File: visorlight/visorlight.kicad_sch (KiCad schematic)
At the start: 1 part

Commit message: rename
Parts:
- added J1: Conn_01x04, Connector_Wire:SolderWire-0.25sqmm_1x01_D0.65mm_OD1.7mm, symbol Connector_Generic:Conn_01x04
- LED1: symbol project_parts:LED_1010RGBC -> visorlight_parts:LED_1010RGBC
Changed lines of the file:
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@@
 (kicad_sch (version 20230121) (generator eeschema)
   (paper "A4")
-  (symbol (lib_id "project_parts:LED_1010RGBC") (at 49.53 46.99 0) (unit 1)
+  (symbol (lib_id "Connector_Generic:Conn_01x04") (at 31.75 48.26 180) (unit 1)
+    (in_bom yes) (on_board yes) (dnp no) (fields_autoplaced)
+    (property "Reference" "J1" (at 31.75 36.83 0)
+      (effects (font (size 1.27 1.27)))
+    )
+    (property "Value" "Conn_01x04" (at 31.75 39.37 0)
+      (effects (font (size 1.27 1.27)))
+    )
+    (property "Footprint" "Connector_Wire:SolderWire-0.25sqmm_1x01_D0.65mm_OD1.7mm" (at 31.75 48.26 0)
+      (effects (font (size 1.27 1.27)) hide)
+    )
+    (property "Datasheet" "~" (at 31.75 48.26 0)
+      (effects (font (size 1.27 1.27)) hide)
+    )
+    (pin "4")
+    (pin "2")
+    (pin "1")
+    (pin "3")
+    (instances
+      (project "visorlight"
+        (path "/ada48de3-1b88-4013-bdaa-c0c1b764bc21"
+          (reference "J1") (unit 1)
+        )
+      )
+    )
+  )
+  (symbol (lib_id "visorlight_parts:LED_1010RGBC") (at 49.53 46.99 0) (unit 1)
     (in_bom yes) (on_board yes) (dnp no)
     (property "Reference" "LED1" (at 44.45 40.64 0)

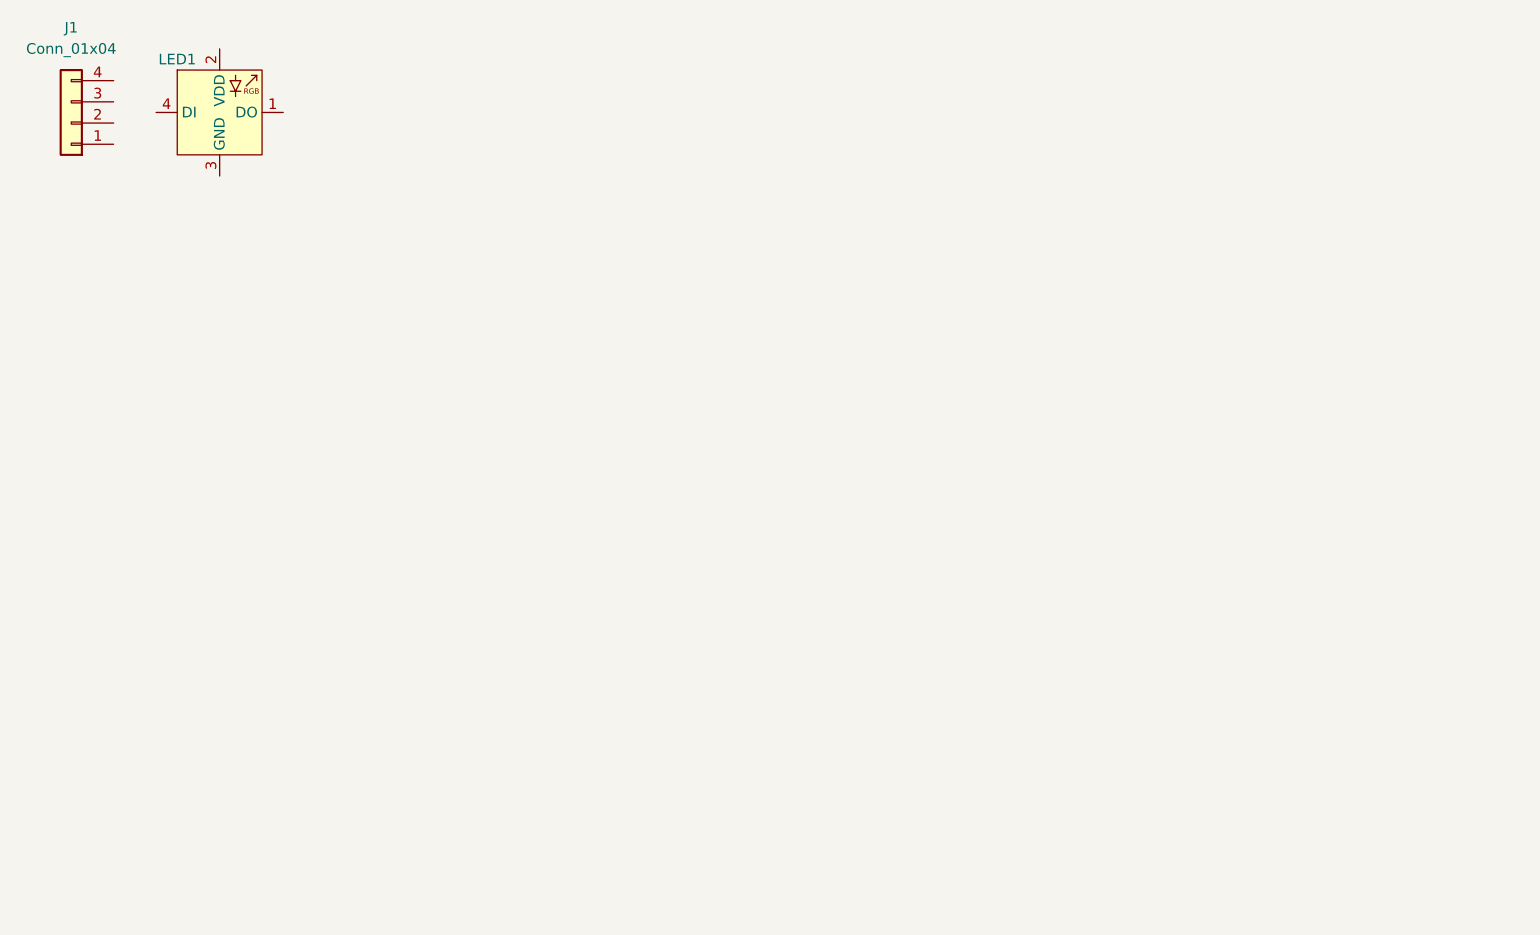
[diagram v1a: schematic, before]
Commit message: moar leds
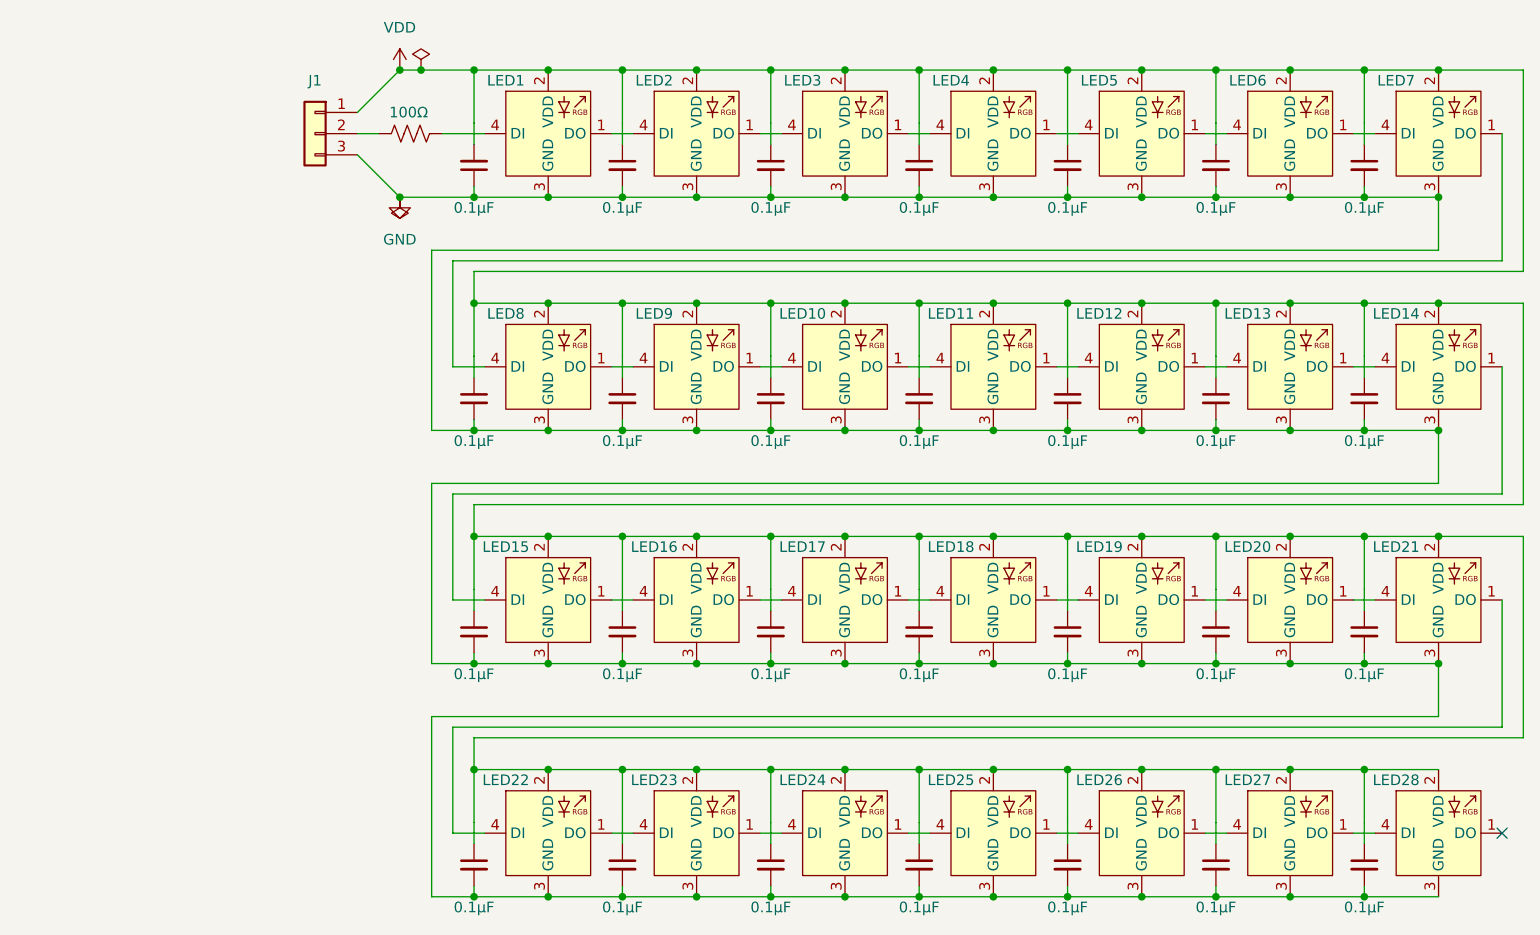
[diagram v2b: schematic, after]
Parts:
- removed J1: Conn_01x04, Connector_Wire:SolderWire-0.25sqmm_1x01_D0.65mm_OD1.7mm, symbol Connector_Generic:Conn_01x04
- added C1, C10, C11, C12, C13, C14, C15, C16, C17, C18, C19, C2, C20, C21, C22, C23, C24, C25, C26, C27, C28, C3, C4, C5, C6, C7, C8, C9: 0.1µF, Capacitor_SMD:C_0603_1608Metric, symbol Device:C_Small
- added J1: Conn_01x03, visorlight_parts:Wires_3x_Relief, symbol Connector_Generic:Conn_01x03
- added LED10, LED11, LED12, LED13, LED14, LED15, LED16, LED17, LED18, LED19, LED2, LED20, LED21, LED22, LED23, LED24, LED25, LED26, LED27, LED28, LED3, LED4, LED5, LED6, LED7, LED8, LED9: ~, visorlight_parts:LED_1010RGBC, symbol visorlight_parts:LED_1010RGBC
- added R1: 100Ω, Resistor_SMD:R_0402_1005Metric, symbol Device:R_US
- LED1: footprint project_parts:LED_1010RGBC -> visorlight_parts:LED_1010RGBC
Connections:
- net at LED1.1 (DO): now also LED2.4 (DI)
- net VDD: now reaches LED1.2 (VDD)
- net VDD: now also C1.2, C10.1, C11.1, C12.1, C13.1, C14.1, C15.1, C16.1, C17.1, C18.1, C19.1, C2.1, C20.1, C21.1, C22.1, C23.1, C24.1, C25.1, C26.1, C27.1, C28.1, C3.1, C4.1, C5.1, C6.1, C7.1, C8.1, C9.1, J1.1 (Pin_1), LED10.2 (VDD), LED11.2 (VDD), LED12.2 (VDD), LED13.2 (VDD), LED14.2 (VDD), LED15.2 (VDD), LED16.2 (VDD), LED17.2 (VDD), LED18.2 (VDD), LED19.2 (VDD), LED2.2 (VDD), LED20.2 (VDD), LED21.2 (VDD), LED22.2 (VDD), LED23.2 (VDD), LED24.2 (VDD), LED25.2 (VDD), LED26.2 (VDD), LED27.2 (VDD), LED28.2 (VDD), LED3.2 (VDD), LED4.2 (VDD), LED5.2 (VDD), LED6.2 (VDD), LED7.2 (VDD), LED8.2 (VDD), LED9.2 (VDD)
- net GND: now reaches LED1.3 (GND)
- net GND: now also C1.1, C10.2, C11.2, C12.2, C13.2, C14.2, C15.2, C16.2, C17.2, C18.2, C19.2, C2.2, C20.2, C21.2, C22.2, C23.2, C24.2, C25.2, C26.2, C27.2, C28.2, C3.2, C4.2, C5.2, C6.2, C7.2, C8.2, C9.2, J1.3 (Pin_3), LED10.3 (GND), LED11.3 (GND), LED12.3 (GND), LED13.3 (GND), LED14.3 (GND), LED15.3 (GND), LED16.3 (GND), LED17.3 (GND), LED18.3 (GND), LED19.3 (GND), LED2.3 (GND), LED20.3 (GND), LED21.3 (GND), LED22.3 (GND), LED23.3 (GND), LED24.3 (GND), LED25.3 (GND), LED26.3 (GND), LED27.3 (GND), LED28.3 (GND), LED3.3 (GND), LED4.3 (GND), LED5.3 (GND), LED6.3 (GND), LED7.3 (GND), LED8.3 (GND), LED9.3 (GND)
- net at LED1.4 (DI): now also R1.1
- new net: LED24.1 (DO), LED25.4 (DI)
- new net: LED23.1 (DO), LED24.4 (DI)
- new net: LED10.1 (DO), LED11.4 (DI)
- new net: LED10.4 (DI), LED9.1 (DO)
- new net: LED7.1 (DO), LED8.4 (DI)
- new net: LED6.1 (DO), LED7.4 (DI)
- new net: LED5.1 (DO), LED6.4 (DI)
- new net: LED4.1 (DO), LED5.4 (DI)
- new net: LED15.1 (DO), LED16.4 (DI)
- new net: LED14.1 (DO), LED15.4 (DI)
- new net: LED27.1 (DO), LED28.4 (DI)
- new net: LED26.1 (DO), LED27.4 (DI)
- new net: LED25.1 (DO), LED26.4 (DI)
- new net: LED12.1 (DO), LED13.4 (DI)
- new net: LED11.1 (DO), LED12.4 (DI)
- new net: LED17.1 (DO), LED18.4 (DI)
- new net: LED16.1 (DO), LED17.4 (DI)
- new net: LED13.1 (DO), LED14.4 (DI)
- new net: LED20.1 (DO), LED21.4 (DI)
- new net: LED19.1 (DO), LED20.4 (DI)
- new net: LED3.1 (DO), LED4.4 (DI)
- new net: LED2.1 (DO), LED3.4 (DI)
- new net: J1.2 (Pin_2), R1.2
- new net: LED18.1 (DO), LED19.4 (DI)
- new net: LED22.1 (DO), LED23.4 (DI)
- new net: LED8.1 (DO), LED9.4 (DI)
- new net: LED21.1 (DO), LED22.4 (DI)
- no-connect marks 0 -> 1
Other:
- moved on the sheet: LED1
